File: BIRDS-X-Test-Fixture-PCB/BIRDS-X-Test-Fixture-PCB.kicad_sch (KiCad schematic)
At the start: 36 parts, among them J101 LPC-50M2LG, J102 Conn_01x05, J105 Conn_01x06, J109 Conn_01x05, J110 Conn_02x05_Odd_Even, J111 Conn_02x05_Odd_Even, SW401 SW_Push

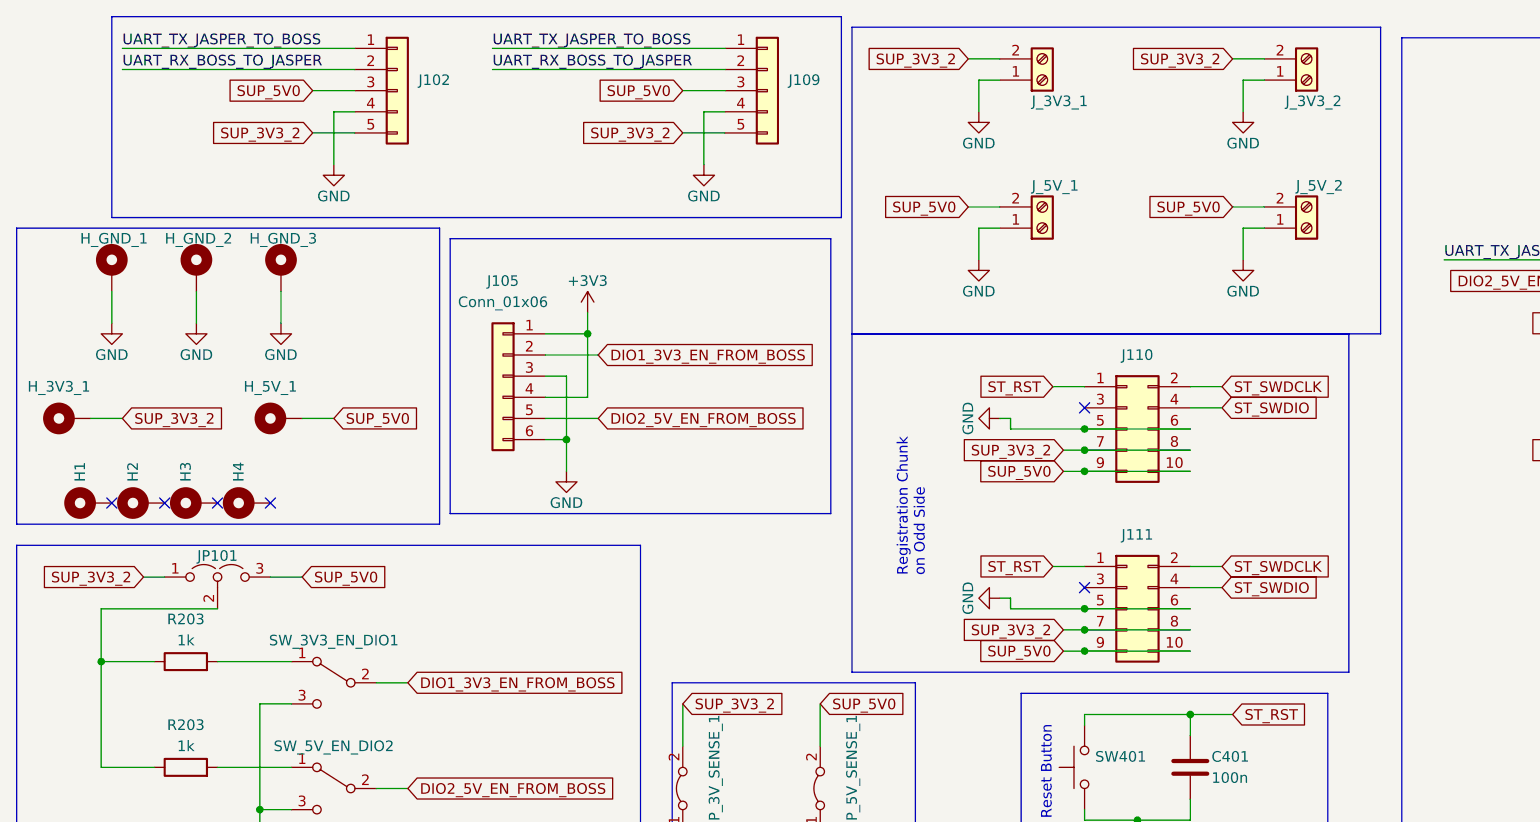
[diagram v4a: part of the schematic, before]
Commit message: Update test fixture board
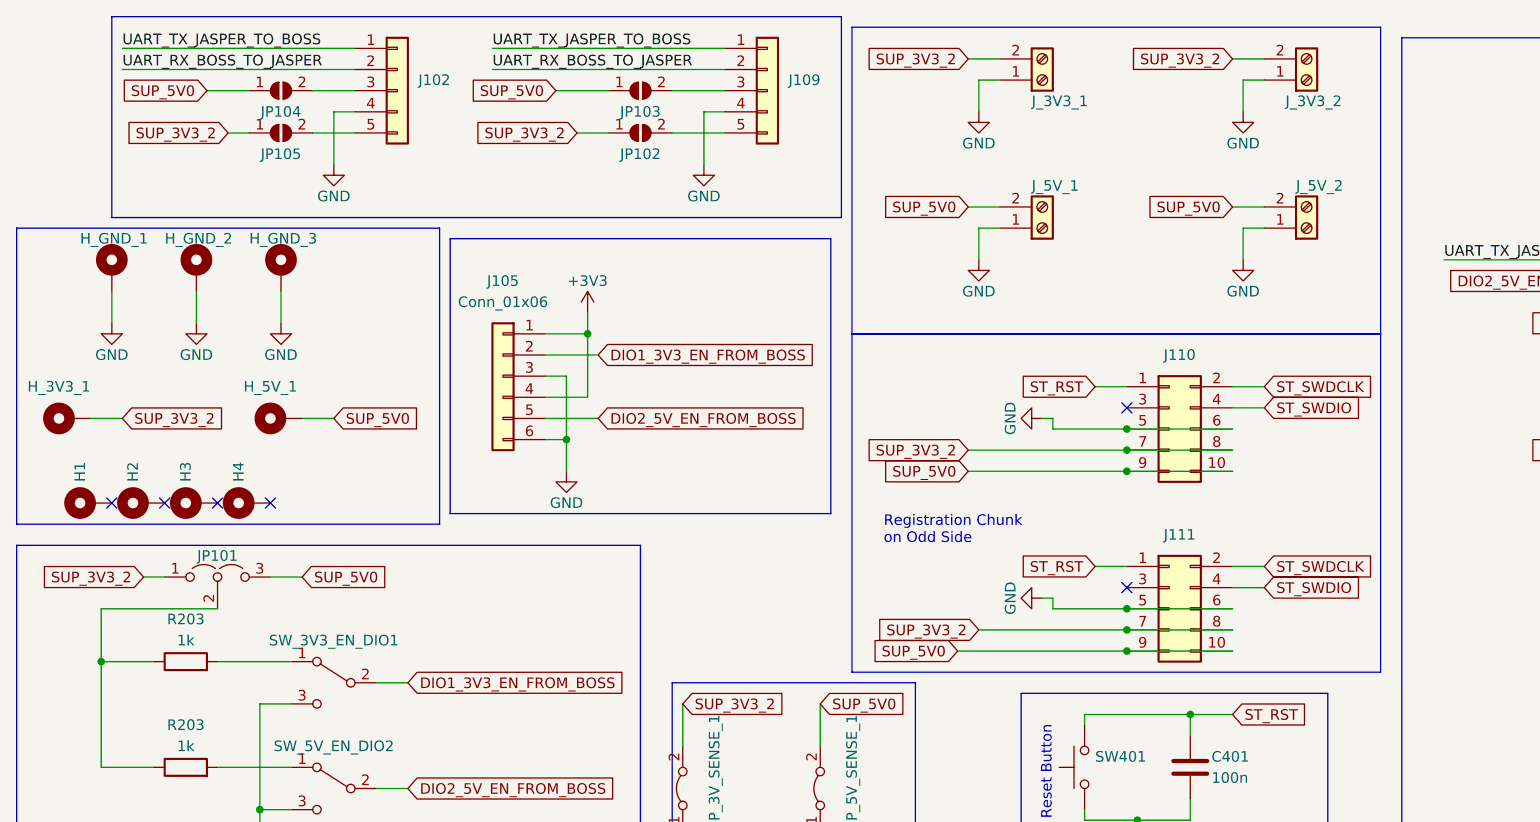
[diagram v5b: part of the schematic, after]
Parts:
- added JP102, JP103, JP104, JP105: SolderJumper_2_Open, Jumper:SolderJumper-2_P1.3mm_Open_RoundedPad1.0x1.5mm, symbol Jumper:SolderJumper_2_Open
- H_3V3_1, H_3V3_DUT_1, H_5V_1, H_5V_DUT_1, H_GND_1, H_GND_2, H_GND_3: footprint MountingHole:MountingHole_4mm_Pad_Via -> 0TestFixtureFootprintLib:EdgeAlligatorConnector
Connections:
- net +3V3: now also JP102.1 (A), JP105.1 (A); no longer J102.5 (Pin_5), J109.5 (Pin_5)
- net +5V: now also JP103.1 (A), JP104.1 (A); no longer J102.3 (Pin_3), J109.3 (Pin_3)
- new net: J109.3 (Pin_3), JP103.2 (B)
- new net: J109.5 (Pin_5), JP102.2 (B)
- new net: J102.5 (Pin_5), JP105.2 (B)
- new net: J102.3 (Pin_3), JP104.2 (B)
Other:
- moved on the sheet: J110, J111

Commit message: Touch up test fixture board
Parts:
- JP_3V_SENSE_1, JP_5V_SENSE_1: footprint TestPoint:TestPoint_2Pads_Pitch2.54mm_Drill0.8mm -> Connector_PinHeader_2.54mm:PinHeader_1x02_P2.54mm_Vertical
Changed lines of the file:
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@@
       (effects (font (size 1.27 1.27)) (justify right) hide)
     )
-    (property "Footprint" "TestPoint:TestPoint_2Pads_Pitch2.54mm_Drill0.8mm" (at 110.49 105.41 0)
+    (property "Footprint" "Connector_PinHeader_2.54mm:PinHeader_1x02_P2.54mm_Vertical" (at 110.49 105.41 0)
       (effects (font (size 1.27 1.27)) hide)
     )
@@
       (effects (font (size 1.27 1.27)) (justify right) hide)
     )
-    (property "Footprint" "TestPoint:TestPoint_2Pads_Pitch2.54mm_Drill0.8mm" (at 93.98 105.41 0)
-      (effects (font (size 1.27 1.27)) hide)
-    )
+    (property "Footprint" "Connector_PinHeader_2.54mm:PinHeader_1x02_P2.54mm_Vertical" (at 93.98 105.41 0)
+      (effects (font (size 1.27 1.27)) hide)
+    )

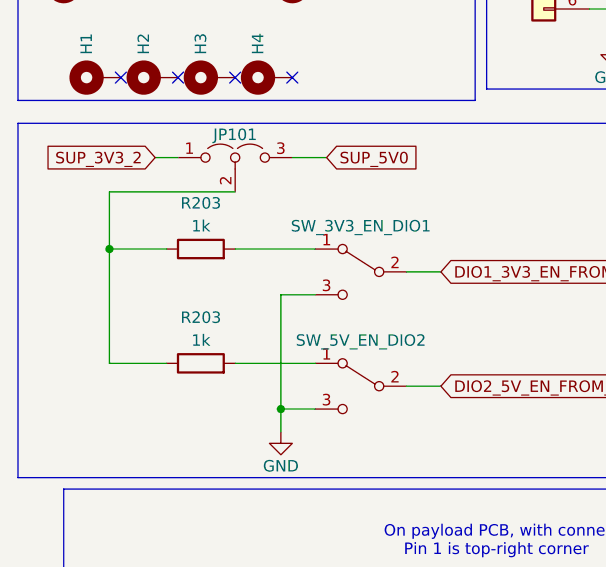
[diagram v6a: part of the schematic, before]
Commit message: Test fixture - update resistor values, add stand offs
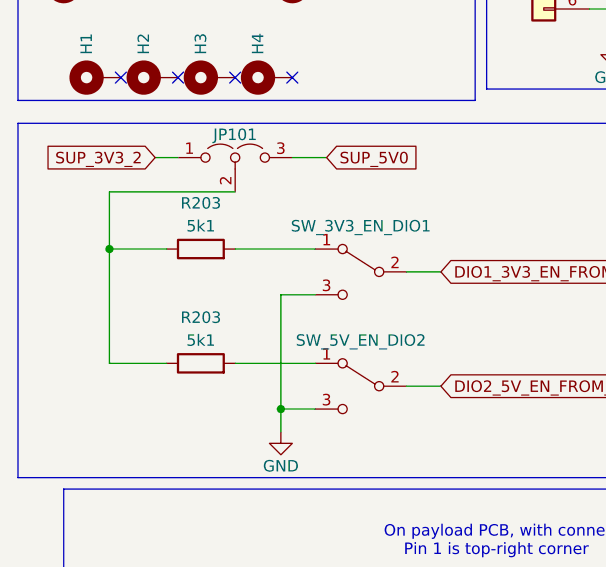
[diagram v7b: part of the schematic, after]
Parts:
- R203: value 1k -> 5k1
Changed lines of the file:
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@@
       (effects (font (size 1.27 1.27)))
     )
-    (property "Value" "1k" (at 34.29 87.63 90)
+    (property "Value" "5k1" (at 34.29 87.63 90)
       (effects (font (size 1.27 1.27)))
     )
@@
       (effects (font (size 1.27 1.27)))
     )
-    (property "Value" "1k" (at 34.29 100.33 90)
-      (effects (font (size 1.27 1.27)))
-    )
+    (property "Value" "5k1" (at 34.29 100.33 90)
+      (effects (font (size 1.27 1.27)))
+    )
